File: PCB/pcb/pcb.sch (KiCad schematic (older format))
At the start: 148 parts, among them J1 USB_B_Micro, U1 ATmega32U4-AU, Y1 16MHz

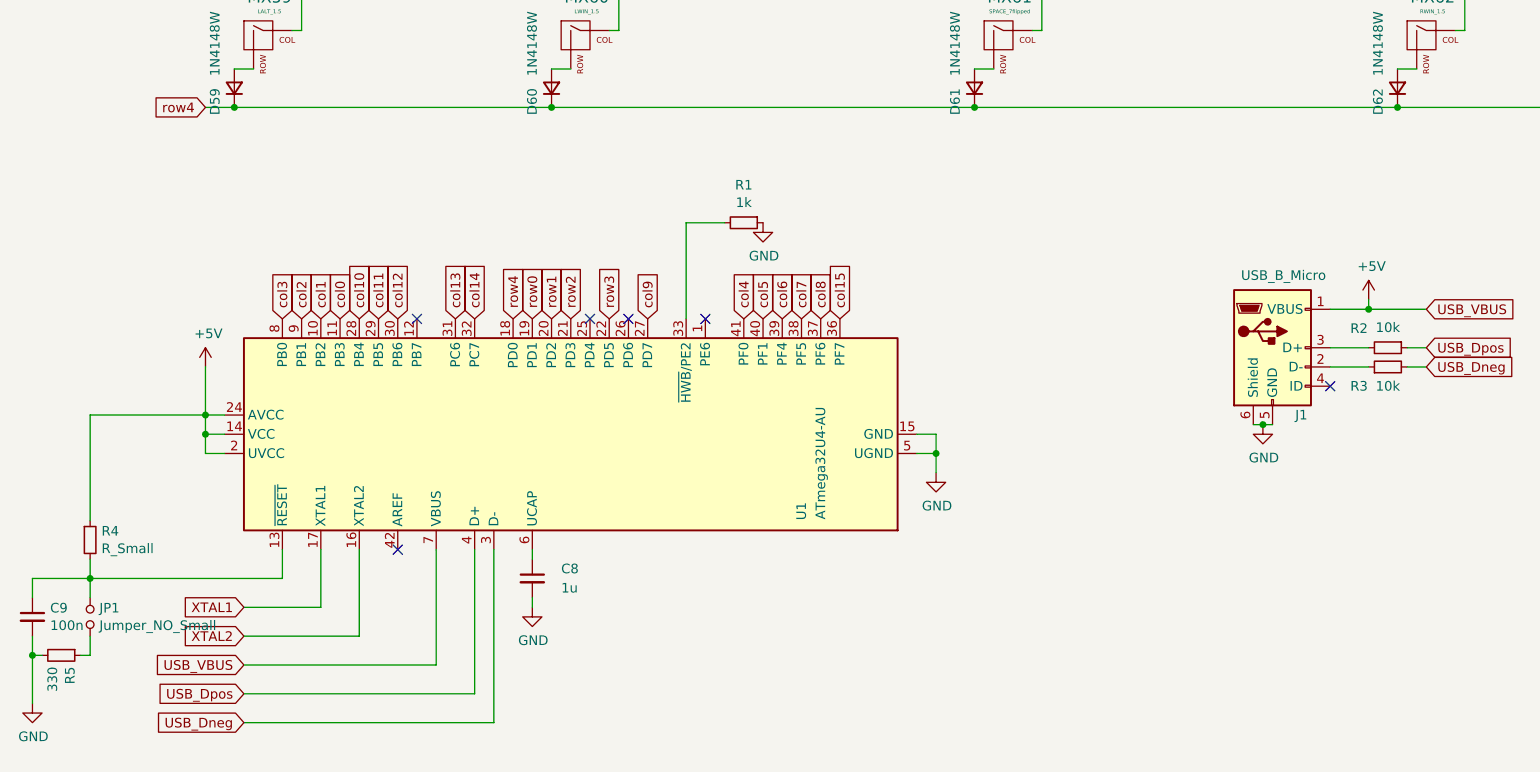
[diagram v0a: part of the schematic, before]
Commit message: Add and ICSP connector and change some values
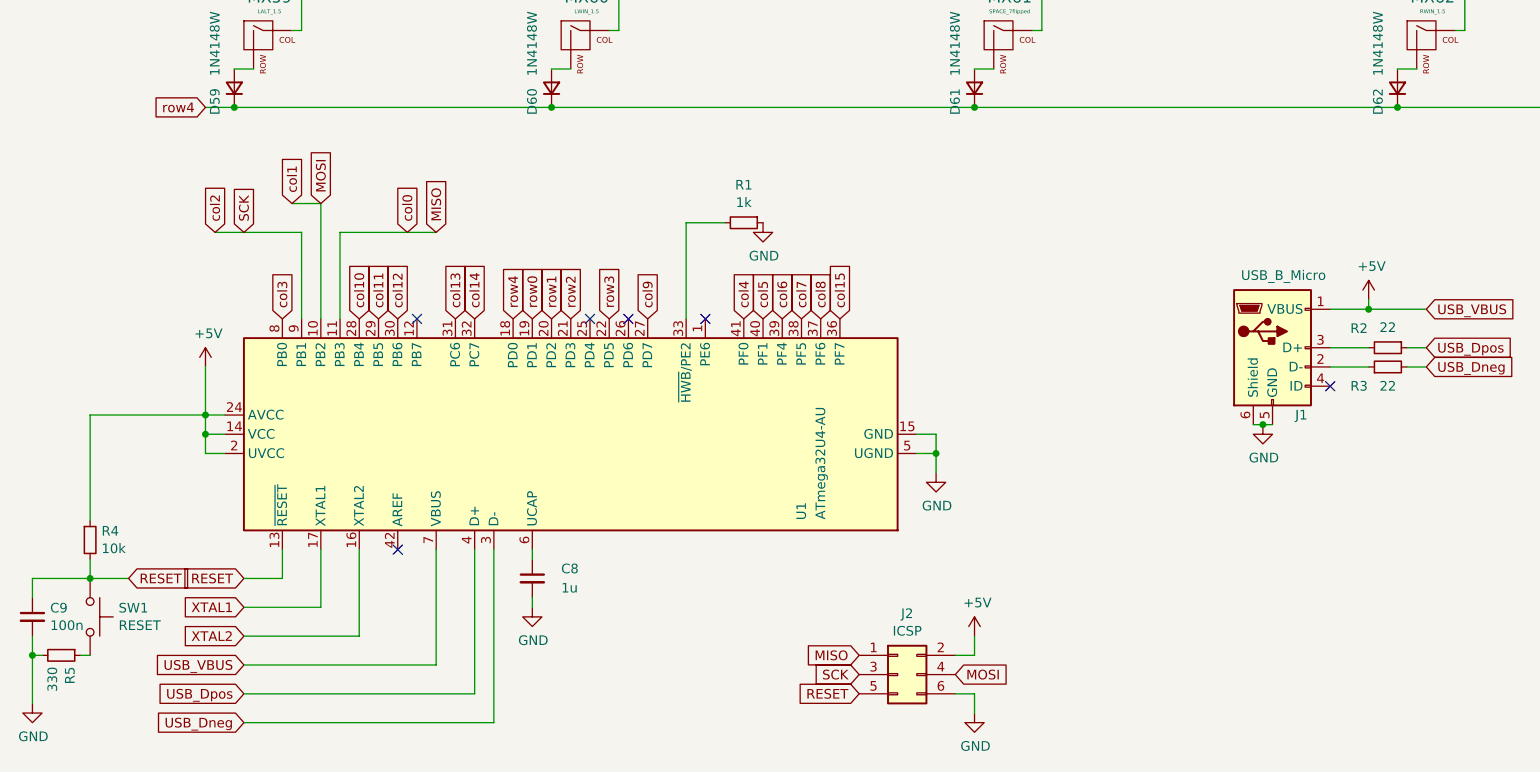
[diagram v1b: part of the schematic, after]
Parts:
- removed JP1: Jumper_NO_Small, Jumper:SolderJumper-2_P1.3mm_Open_RoundedPad1.0x1.5mm, symbol Device:Jumper_NO_Small
- added J2: ICSP, symbol Connector_Generic:Conn_02x03_Odd_Even
- added SW1: RESET, symbol Switch:SW_Push
- R2, R3: value 10k -> 22
- R4: value R_Small -> 10k
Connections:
- net +5V: now also J2.2 (Pin_2)
- net GND: now also J2.6 (Pin_6)
- net RESET: now reaches C9.1, R4.2, U1.13 (~RESET)
- net RESET: now also J2.5 (Pin_5), SW1.1
- net at R5.1: now also SW1.2
- net col0 renamed MISO
- net MISO: now also J2.1 (Pin_1)
- net col1 renamed MOSI
- net MOSI: now also J2.4 (Pin_4)
- net col2 renamed SCK
- net SCK: now also J2.3 (Pin_3)
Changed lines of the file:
@@
 P 7800 5550
 F 0 "R2" V 7700 5400 50  0000 C CNN
-F 1 "10k" V 7695 5550 50  0000 C CNN
+F 1 "22" V 7695 5550 50  0000 C CNN
 F 2 "Resistor_SMD:R_1206_3216Metric_Pad1.42x1.75mm_HandSolder" H 7800 5550 50  0001 C CNN
 F 3 "~" H 7800 5550 50  0001 C CNN
@@
 P 7800 5650
 F 0 "R3" V 7700 5800 50  0000 C CNN
-F 1 "10k" V 7700 5650 50  0000 C CNN
+F 1 "22" V 7700 5650 50  0000 C CNN
 F 2 "Resistor_SMD:R_1206_3216Metric_Pad1.42x1.75mm_HandSolder" H 7800 5650 50  0001 C CNN
 F 3 "~" H 7800 5650 50  0001 C CNN
@@
 P 1050 6550
 F 0 "R4" H 1109 6596 50  0000 L CNN
-F 1 "R_Small" H 1109 6505 50  0000 L CNN
+F 1 "10k" H 1109 6505 50  0000 L CNN
 F 2 "Resistor_SMD:R_1206_3216Metric_Pad1.42x1.75mm_HandSolder" H 1050 6550 50  0001 C CNN
 F 3 "~" H 1050 6550 50  0001 C CNN
@@
 $EndComp
 Connection ~ 9300 6300
-Wire Wire Line
-	1050 6750 2050 6750
 Wire Wire Line
 	1050 6450 1050 5900
@@
 Wire Wire Line
 	7150 5950 7200 5950
-Text GLabel 2150 5400 1    50   Input ~ 0
+Text GLabel 1700 4950 1    50   Input ~ 0
 col2
-Text GLabel 2250 5400 1    50   Input ~ 0
+Text GLabel 2100 4800 1    50   Input ~ 0
 col1
-Text GLabel 2350 5400 1    50   Input ~ 0
+Text GLabel 2700 4950 1    50   Input ~ 0
 col0
 $Comp
@@
 $EndComp
 $Comp
-L Device:Jumper_NO_Small JP1
-U 1 1 5E4BD970
+L Connector_Generic:Conn_02x03_Odd_Even J2
+U 1 1 5E528F69
+P 5250 7250
+F 0 "J2" H 5300 7567 50  0000 C CNN
+F 1 "ICSP" H 5300 7476 50  0000 C CNN
+F 2 "" H 5250 7250 50  0001 C CNN
+F 3 "~" H 5250 7250 50  0001 C CNN
+	1    5250 7250
+	1    0    0    -1
+$EndComp
+$Comp
+L Switch:SW_Push SW1
+U 1 1 5E56EAEA
 P 1050 6950
-F 0 "JP1" V 1004 6998 50  0000 L CNN
-F 1 "Jumper_NO_Small" V 1095 6998 50  0000 L CNN
-F 2 "Jumper:SolderJumper-2_P1.3mm_Open_RoundedPad1.0x1.5mm" H 1050 6950 50  0001 C CNN
-F 3 "~" H 1050 6950 50  0001 C CNN
+F 0 "SW1" V 1004 7098 50  0000 L CNN
+F 1 "RESET" V 1095 7098 50  0000 L CNN
+F 2 "" H 1050 7150 50  0001 C CNN
+F 3 "~" H 1050 7150 50  0001 C CNN
 	1    1050 6950
 	0    1    1    0
 $EndComp
-Wire Wire Line
-	1050 6750 1050 6850
-Wire Wire Line
-	1050 7150 1050 7050
+$Comp
+L power:+5V #PWR0103
+U 1 1 5E5B4488
+P 5650 7050
+F 0 "#PWR0103" H 5650 6900 50  0001 C CNN
+F 1 "+5V" H 5665 7223 50  0000 C CNN
+F 2 "" H 5650 7050 50  0001 C CNN
+F 3 "" H 5650 7050 50  0001 C CNN
+	1    5650 7050
+	1    0    0    -1
+$EndComp
+Wire Wire Line
+	5550 7150 5650 7150
+Wire Wire Line
+	5650 7150 5650 7050
+$Comp
+L power:GND #PWR0104
+U 1 1 5E5D708B
+P 5650 7450
+F 0 "#PWR0104" H 5650 7200 50  0001 C CNN
+F 1 "GND" H 5655 7277 50  0000 C CNN
+F 2 "" H 5650 7450 50  0001 C CNN
+F 3 "" H 5650 7450 50  0001 C CNN
+	1    5650 7450
+	1    0    0    -1
+$EndComp
+Wire Wire Line
+	5550 7350 5650 7350
+Wire Wire Line
+	5650 7350 5650 7450
+Text GLabel 2850 4950 1    50   Input ~ 0
+MISO
+Text GLabel 5050 7150 0    50   Input ~ 0
+MISO
+Text GLabel 5050 7250 0    50   Input ~ 0
+SCK
+Text GLabel 1850 4950 1    50   Input ~ 0
+SCK
+Wire Wire Line
+	1700 4950 2150 4950
+Wire Wire Line
+	2150 4950 2150 5400
+Text GLabel 5050 7350 0    50   Input ~ 0
+RESET
+Text GLabel 1850 6750 0    50   Input ~ 0
+RESET
+Text GLabel 1250 6750 2    50   Input ~ 0
+RESET
+Wire Wire Line
+	1050 6750 1250 6750
+Wire Wire Line
+	1850 6750 2050 6750
+Text GLabel 5550 7250 2    50   Input ~ 0
+MOSI
+Wire Wire Line
+	2350 4950 2850 4950
+Wire Wire Line
+	2350 4950 2350 5400
+Text GLabel 2250 4800 1    50   Input ~ 0
+MOSI
+Wire Wire Line
+	2100 4800 2250 4800
+Wire Wire Line
+	2250 4800 2250 5400
 $EndSCHEMATC

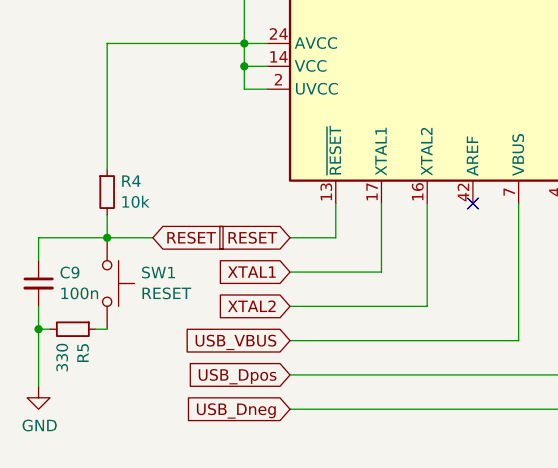
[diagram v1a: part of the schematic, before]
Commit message: Move the USB port and regenerate the Gerbers
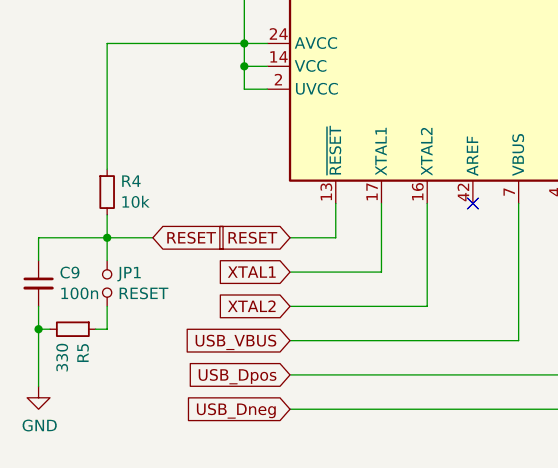
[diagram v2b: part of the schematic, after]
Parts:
- removed SW1: RESET, symbol Switch:SW_Push
- added JP1: RESET, Connector_PinSocket_2.54mm:PinSocket_1x02_P2.54mm_Vertical, symbol Device:Jumper_NO_Small
- J2: footprint (none) -> Connector_PinHeader_2.54mm:PinHeader_2x03_P2.54mm_Vertical
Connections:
- net RESET: now also JP1.1
- net at R5.1: now also JP1.2
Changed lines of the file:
@@
 F 0 "J2" H 5300 7567 50  0000 C CNN
 F 1 "ICSP" H 5300 7476 50  0000 C CNN
-F 2 "" H 5250 7250 50  0001 C CNN
+F 2 "Connector_PinHeader_2.54mm:PinHeader_2x03_P2.54mm_Vertical" H 5250 7250 50  0001 C CNN
 F 3 "~" H 5250 7250 50  0001 C CNN
 	1    5250 7250
 	1    0    0    -1
-$EndComp
-$Comp
-L Switch:SW_Push SW1
-U 1 1 5E56EAEA
-P 1050 6950
-F 0 "SW1" V 1004 7098 50  0000 L CNN
-F 1 "RESET" V 1095 7098 50  0000 L CNN
-F 2 "" H 1050 7150 50  0001 C CNN
-F 3 "~" H 1050 7150 50  0001 C CNN
-	1    1050 6950
-	0    1    1    0
 $EndComp
 $Comp
@@
 Wire Wire Line
 	2250 4800 2250 5400
+$Comp
+L Device:Jumper_NO_Small JP1
+U 1 1 5E565D73
+P 1050 6950
+F 0 "JP1" V 1004 6998 50  0000 L CNN
+F 1 "RESET" V 1095 6998 50  0000 L CNN
+F 2 "Connector_PinSocket_2.54mm:PinSocket_1x02_P2.54mm_Vertical" H 1050 6950 50  0001 C CNN
+F 3 "~" H 1050 6950 50  0001 C CNN
+	1    1050 6950
+	0    1    1    0
+$EndComp
+Wire Wire Line
+	1050 7050 1050 7150
+Wire Wire Line
+	1050 6850 1050 6750
 $EndSCHEMATC

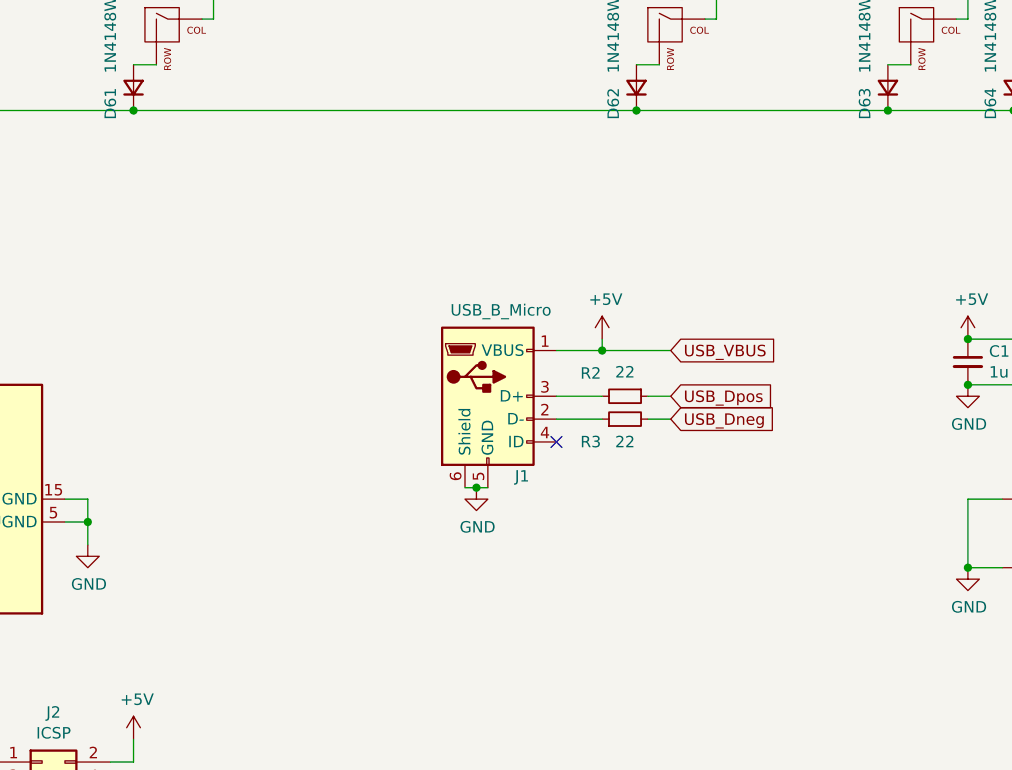
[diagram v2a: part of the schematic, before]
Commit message: Add ESD Protection and make sure the fill zones are on both sides of the board
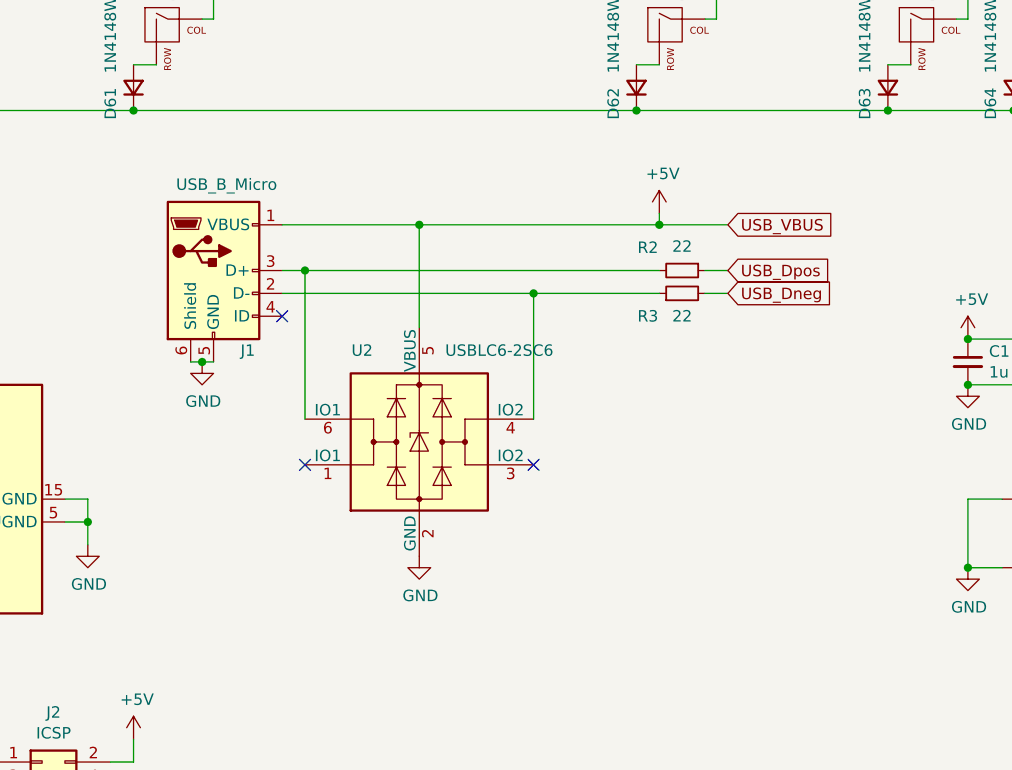
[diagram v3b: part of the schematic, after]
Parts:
- added U2: USBLC6-2SC6, Package_TO_SOT_SMD:SOT-23-6, symbol Power_Protection:USBLC6-2SC6
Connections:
- net +5V: now also U2.5 (VBUS)
- net GND: now also U2.2 (GND)
- net at J1.3 (D+), R2.2: now also U2.6 (IO1)
- net at J1.2 (D-), R3.1: now also U2.4 (IO2)
- no-connect marks 7 -> 9
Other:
- moved on the sheet: J1, R2, R3
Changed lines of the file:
@@
 L power:GND #PWR06
 U 1 1 5E45CF9B
-P 7150 5950
-F 0 "#PWR06" H 7150 5700 50  0001 C CNN
-F 1 "GND" H 7155 5777 50  0000 C CNN
-F 2 "" H 7150 5950 50  0001 C CNN
-F 3 "" H 7150 5950 50  0001 C CNN
-	1    7150 5950
+P 5950 5400
+F 0 "#PWR06" H 5950 5150 50  0001 C CNN
+F 1 "GND" H 5955 5227 50  0000 C CNN
+F 2 "" H 5950 5400 50  0001 C CNN
+F 3 "" H 5950 5400 50  0001 C CNN
+	1    5950 5400
 	1    0    0    -1
 $EndComp
@@
 L Connector:USB_B_Micro J1
 U 1 1 5E471F5B
-P 7200 5550
-F 0 "J1" H 7350 5200 50  0000 C CNN
-F 1 "USB_B_Micro" H 7257 5926 50  0000 C CNN
-F 2 "Connector_USB:USB_Micro-B_GCT_USB3076-30-A" H 7350 5500 50  0001 C CNN
-F 3 "~" H 7350 5500 50  0001 C CNN
-	1    7200 5550
+P 6000 5000
+F 0 "J1" H 6150 4650 50  0000 C CNN
+F 1 "USB_B_Micro" H 6057 5376 50  0000 C CNN
+F 2 "Connector_USB:USB_Micro-B_GCT_USB3076-30-A" H 6150 4950 50  0001 C CNN
+F 3 "~" H 6150 4950 50  0001 C CNN
+	1    6000 5000
 	1    0    0    -1
 $EndComp
@@
 L power:+5V #PWR02
 U 1 1 5E472FB9
-P 7700 5300
-F 0 "#PWR02" H 7700 5150 50  0001 C CNN
-F 1 "+5V" H 7715 5473 50  0000 C CNN
-F 2 "" H 7700 5300 50  0001 C CNN
-F 3 "" H 7700 5300 50  0001 C CNN
-	1    7700 5300
-	1    0    0    -1
-$EndComp
-Wire Wire Line
-	7500 5350 7700 5350
-Wire Wire Line
-	7700 5350 7700 5300
+P 7950 4750
+F 0 "#PWR02" H 7950 4600 50  0001 C CNN
+F 1 "+5V" H 7965 4923 50  0000 C CNN
+F 2 "" H 7950 4750 50  0001 C CNN
+F 3 "" H 7950 4750 50  0001 C CNN
+	1    7950 4750
+	1    0    0    -1
+$EndComp
+Wire Wire Line
+	7950 4800 7950 4750
 $Comp
 L Device:R_Small R2
 U 1 1 5E45E85B
-P 7800 5550
-F 0 "R2" V 7700 5400 50  0000 C CNN
-F 1 "22" V 7695 5550 50  0000 C CNN
-F 2 "Resistor_SMD:R_1206_3216Metric_Pad1.42x1.75mm_HandSolder" H 7800 5550 50  0001 C CNN
-F 3 "~" H 7800 5550 50  0001 C CNN
-	1    7800 5550
+P 8050 5000
+F 0 "R2" V 7950 4850 50  0000 C CNN
+F 1 "22" V 7945 5000 50  0000 C CNN
+F 2 "Resistor_SMD:R_1206_3216Metric_Pad1.42x1.75mm_HandSolder" H 8050 5000 50  0001 C CNN
+F 3 "~" H 8050 5000 50  0001 C CNN
+	1    8050 5000
 	0    1    1    0
 $EndComp
@@
 L Device:R_Small R3
 U 1 1 5E45EDA3
-P 7800 5650
-F 0 "R3" V 7700 5800 50  0000 C CNN
-F 1 "22" V 7700 5650 50  0000 C CNN
-F 2 "Resistor_SMD:R_1206_3216Metric_Pad1.42x1.75mm_HandSolder" H 7800 5650 50  0001 C CNN
-F 3 "~" H 7800 5650 50  0001 C CNN
-	1    7800 5650
-	0    -1   -1   0
-$EndComp
-Wire Wire Line
-	7500 5550 7700 5550
-Wire Wire Line
-	7500 5650 7700 5650
-Wire Wire Line
-	7900 5550 8000 5550
-Wire Wire Line
-	7900 5650 8000 5650
-Wire Wire Line
-	7700 5350 8000 5350
-Connection ~ 7700 5350
+P 8050 5100
+F 0 "R3" V 7950 5250 50  0000 C CNN
+F 1 "22" V 7950 5100 50  0000 C CNN
+F 2 "Resistor_SMD:R_1206_3216Metric_Pad1.42x1.75mm_HandSolder" H 8050 5100 50  0001 C CNN
+F 3 "~" H 8050 5100 50  0001 C CNN
+	1    8050 5100
+	0    -1   -1   0
+$EndComp
+Wire Wire Line
+	8150 5000 8250 5000
+Wire Wire Line
+	8150 5100 8250 5100
+Connection ~ 7950 4800
 NoConn ~ 2650 6600
 Wire Wire Line
@@
 Text GLabel 10650 6300 2    50   Input ~ 0
 XTAL2
-Text GLabel 8000 5350 2    50   Input ~ 0
+Text GLabel 8250 4800 2    50   Input ~ 0
 USB_VBUS
-Text GLabel 8000 5550 2    50   Input ~ 0
+Text GLabel 8250 5000 2    50   Input ~ 0
 USB_Dpos
-Text GLabel 8000 5650 2    50   Input ~ 0
+Text GLabel 8250 5100 2    50   Input ~ 0
 USB_Dneg
 Wire Wire Line
@@
 NoConn ~ 4250 5400
 Wire Wire Line
-	7100 5950 7150 5950
-NoConn ~ 7500 5750
-Connection ~ 7150 5950
-Wire Wire Line
-	7150 5950 7200 5950
+	5900 5400 5950 5400
+NoConn ~ 6300 5200
+Connection ~ 5950 5400
+Wire Wire Line
+	5950 5400 6000 5400
 Text GLabel 1700 4950 1    50   Input ~ 0
 col2
@@
 Wire Wire Line
 	1050 6850 1050 6750
+$Comp
+L Power_Protection:USBLC6-2SC6 U2
+U 1 1 5E61B7E3
+P 6900 5750
+F 0 "U2" H 6650 6150 50  0000 C CNN
+F 1 "USBLC6-2SC6" H 7250 6150 50  0000 C CNN
+F 2 "Package_TO_SOT_SMD:SOT-23-6" H 6150 6150 50  0001 C CNN
+F 3 "http://www2.st.com/resource/en/datasheet/CD00050750.pdf" H 7100 6100 50  0001 C CNN
+	1    6900 5750
+	1    0    0    -1
+$EndComp
+$Comp
+L power:GND #PWR0105
+U 1 1 5E64807D
+P 6900 6250
+F 0 "#PWR0105" H 6900 6000 50  0001 C CNN
+F 1 "GND" H 6905 6077 50  0000 C CNN
+F 2 "" H 6900 6250 50  0001 C CNN
+F 3 "" H 6900 6250 50  0001 C CNN
+	1    6900 6250
+	1    0    0    -1
+$EndComp
+Wire Wire Line
+	7950 4800 8250 4800
+Wire Wire Line
+	6300 5100 7400 5100
+Wire Wire Line
+	6300 5000 6400 5000
+Wire Wire Line
+	6300 4800 6900 4800
+Wire Wire Line
+	6400 5650 6400 5000
+Connection ~ 6400 5000
+Wire Wire Line
+	6400 5000 7950 5000
+Wire Wire Line
+	7400 5650 7400 5100
+Connection ~ 7400 5100
+Wire Wire Line
+	7400 5100 7950 5100
+Wire Wire Line
+	6900 5250 6900 4800
+Connection ~ 6900 4800
+Wire Wire Line
+	6900 4800 7950 4800
+NoConn ~ 7400 5850
+NoConn ~ 6400 5850
 $EndSCHEMATC
